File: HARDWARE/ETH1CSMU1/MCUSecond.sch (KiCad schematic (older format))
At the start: 23 parts

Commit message: Added ADC
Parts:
- removed C? (x2): 1u, symbol Device:C
- removed C? (x6): 100n, symbol Device:C
- removed FB? (x2): BEAD, symbol Device:Ferrite_Bead_Small
- removed U?: STM32F765VITx, Package_QFP:LQFP-100_14x14mm_P0.5mm, symbol MCU_ST_STM32F7:STM32F765VITx
- added C201, C203, C204, C205, C206, C207, C210, C211, C214, C215, C216, C217: 100n, symbol Device:C
- added C218: 1u, symbol Device:C
- added C219, C220: 2u2, symbol Device:C
- added FB201: Ferrite_Bead_Small, symbol Device:Ferrite_Bead_Small
- added R205: R, symbol Device:R
- added U202: STM32F746ZGTx, symbol stm32:STM32F746ZGTx
- gave numbers to parts that had none: 12
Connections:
- net labels added: MCU_3V3
- net labels removed: +3V3
- wire segments 146 -> 184
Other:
- moved on the sheet: C208, C209, C212, C213, J201, R202, R203, R204, U201, X201

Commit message: Commit
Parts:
- removed R204: R, symbol Device:R
- added FB202: MPZ2012S221A, SMD:R_0805_Symbol1, symbol Device:Ferrite_Bead_Small
- C201, C202, C203, C204, C205, C206, C207, C210, C211, C214, C215, C216, C217: footprint (none) -> SMD:C_0603_Symbol1
- C212: value 2u7 -> 100n; footprint (none) -> SMD:C_0603_Symbol1
- C213: value 2u7 -> 1u
- FB201: value Ferrite_Bead_Small -> MPZ2012S221A; footprint (none) -> SMD:R_0805_Symbol1
- R201: footprint (none) -> SMD:R_0603_Symbol1
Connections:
- net labels added: SECOND-I2C1_SCL, SECOND-I2C1_SDA, SECOND-NC-TDI, SECOND-NRST, SECOND-SWDCKL-TCK, SECOND-SWDIO-TMS, SECOND-SWO-TDO
- net labels removed: FGEN_FSELECT, FGEN_PSELECT, FGEN_SLEEP, I2C1_SCL, I2C1_SDA, NRST, POLARITY, QDAC_~CLR, QDAC_~LDAC, SIGN_SELECT, SPI2_MISO, SPI2_MOSI, SPI2_NSS, SPI2_SCK, SPI4_MOSI, SPI4_NSS1, SPI4_NSS2, SPI4_NSS3, SPI4_SCK, SPI6_MISO, SPI6_MOSI, SPI6_NSS1, SPI6_NSS2, SPI6_SCK, TCK, TDI, TDO, TMS, VDDA
- wire segments 184 -> 162
- no-connect marks 3 -> 2
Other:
- moved on the sheet: C201, C202, C203, C204, C205, C206, C207, C210, C211, C214, C215, C216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

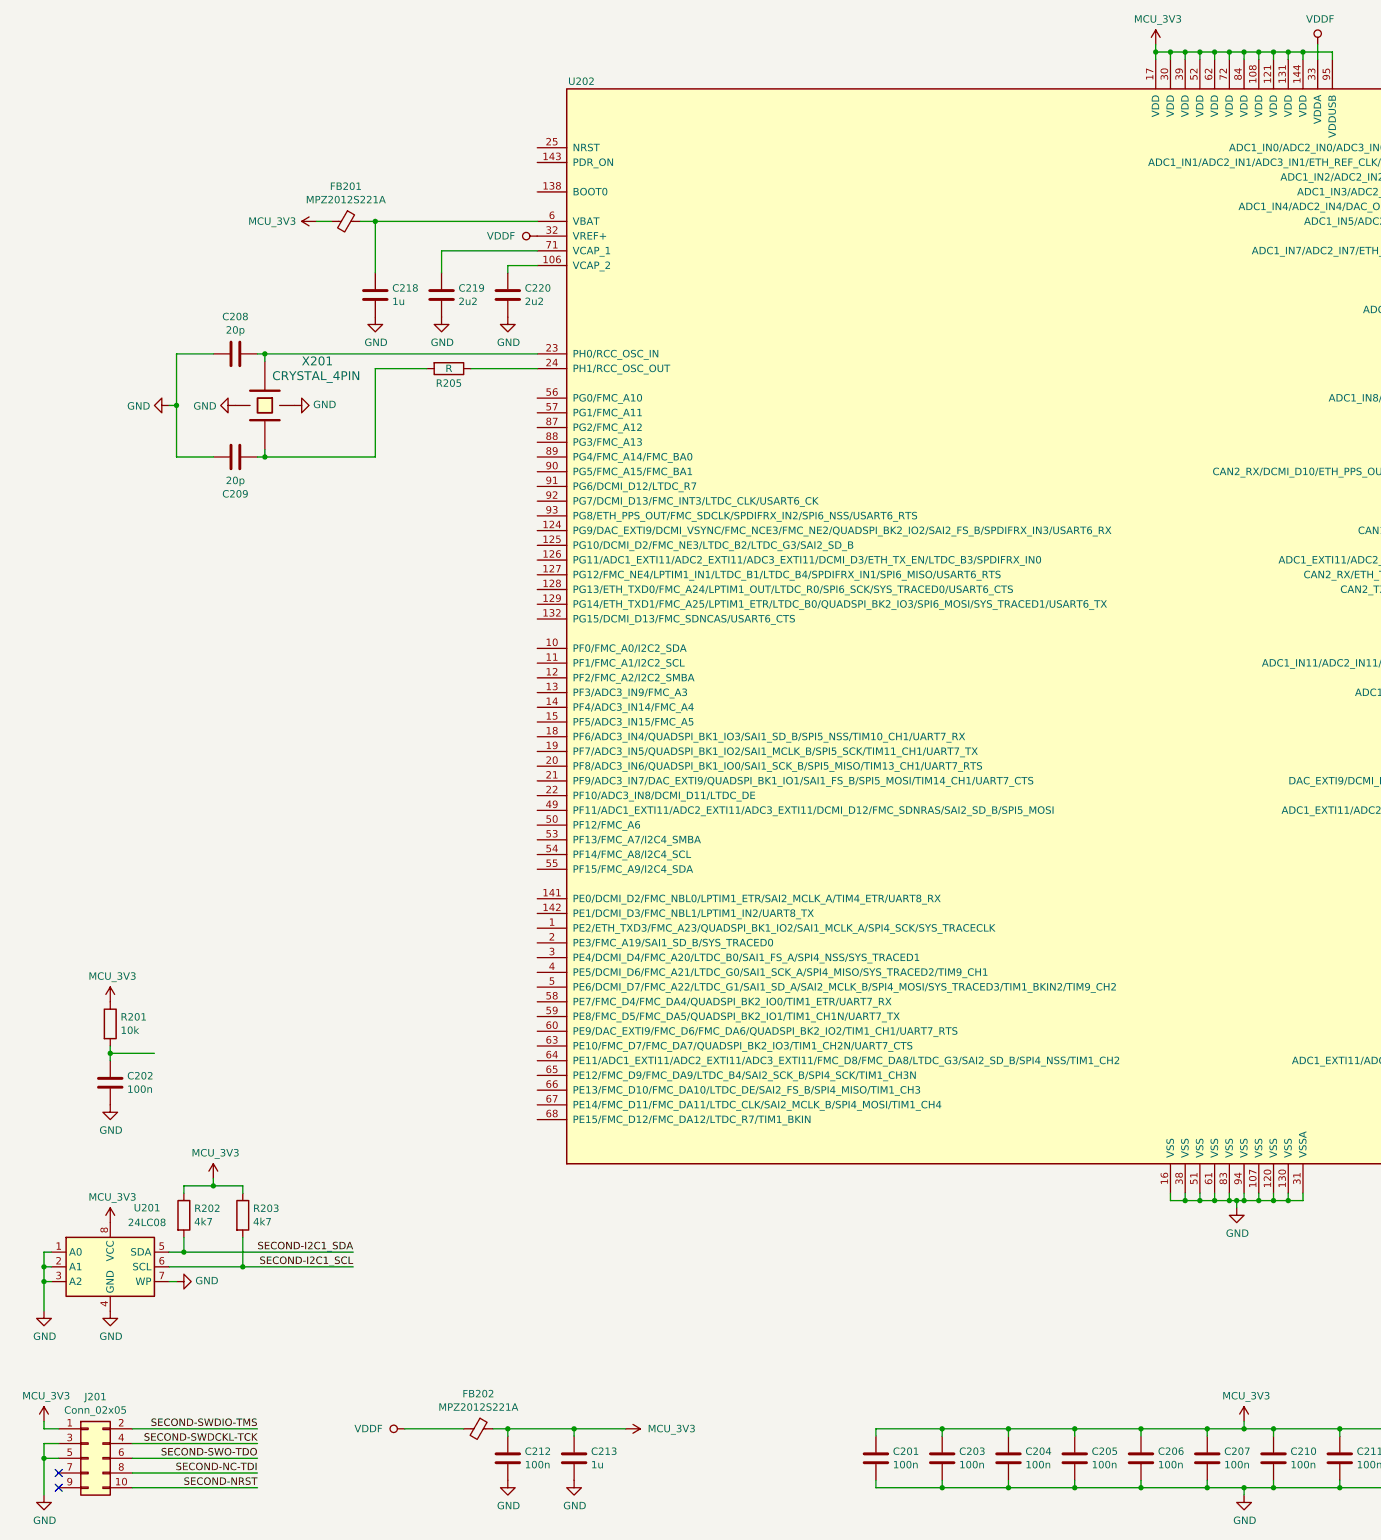
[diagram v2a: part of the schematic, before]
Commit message: Power schematic
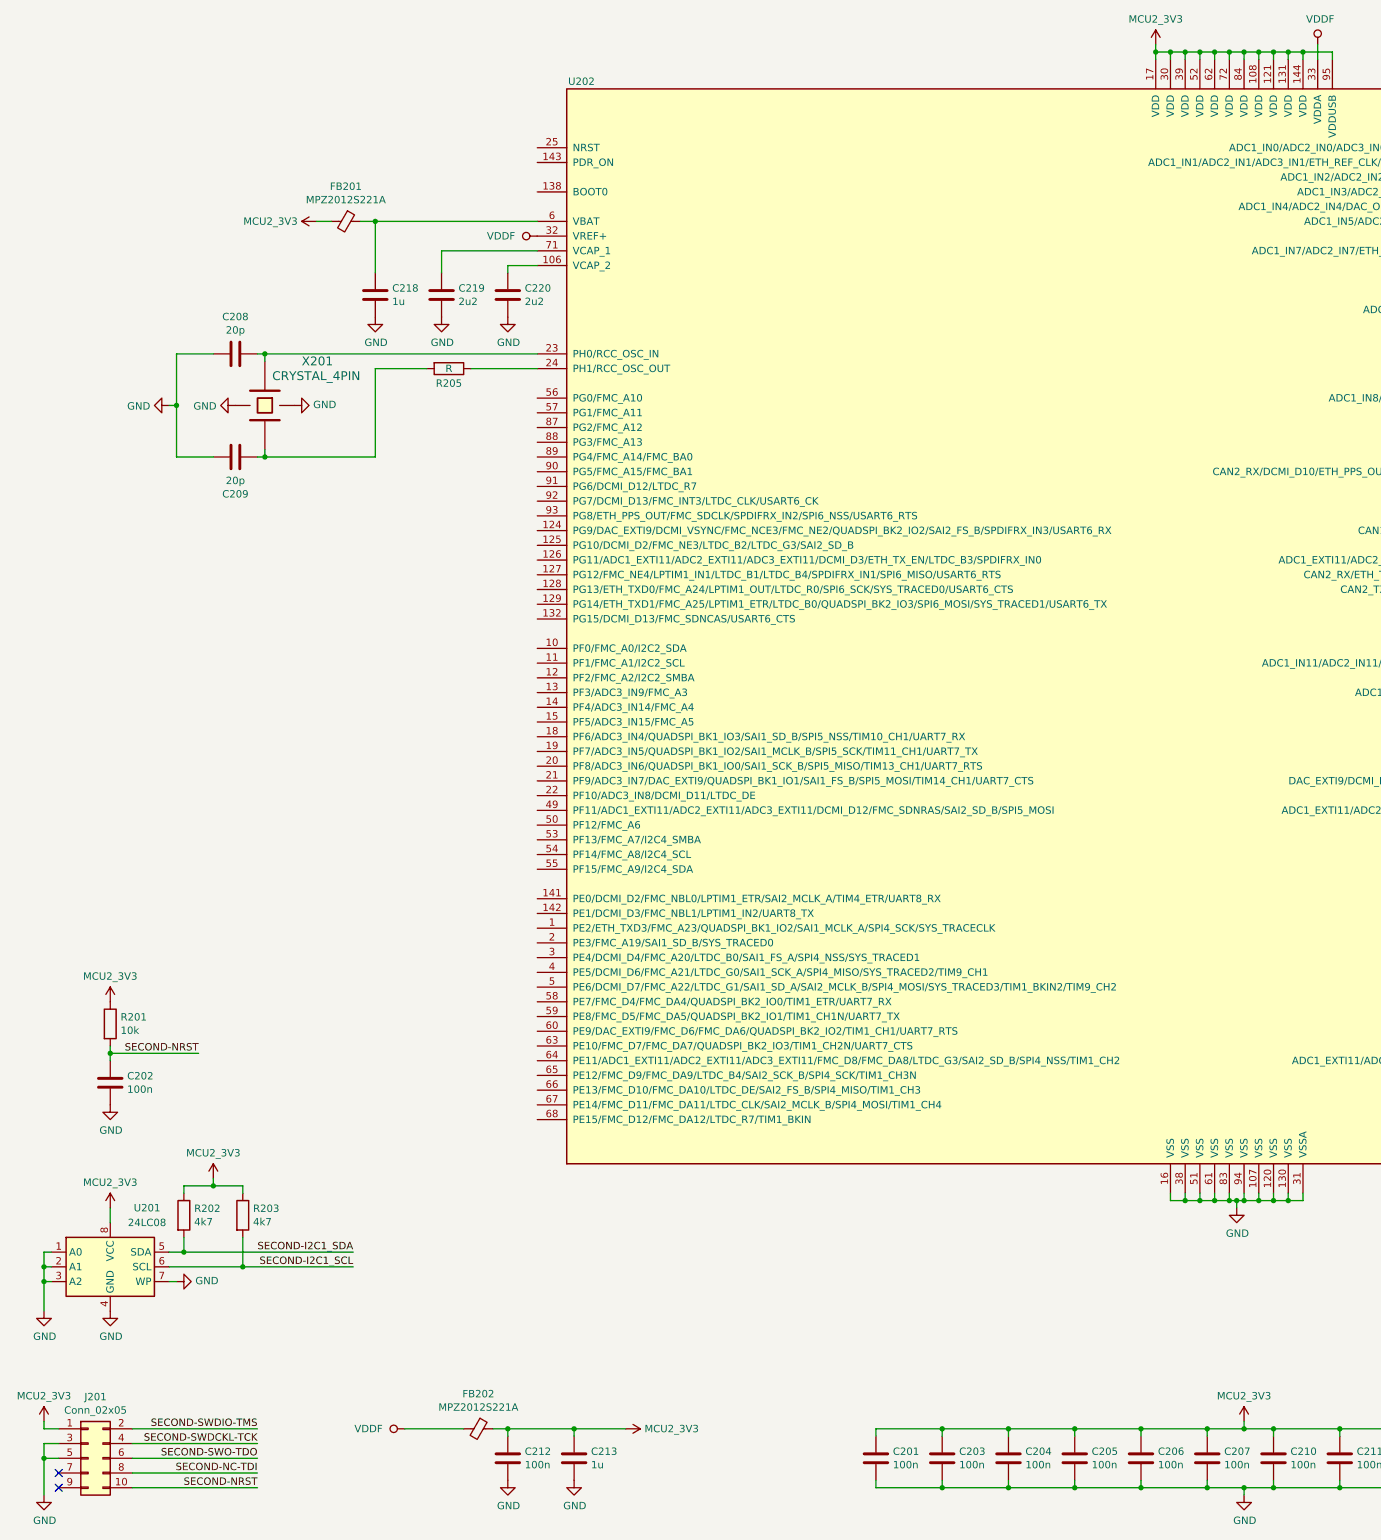
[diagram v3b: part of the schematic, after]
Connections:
- net SECOND-NRST: now also C202.1, R201.2
- net MCU_3V3 renamed MCU2_3V3
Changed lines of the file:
@@
 $Descr A3 16535 11693
 encoding utf-8
-Sheet 2 12
+Sheet 2 13
 Title ""
 Date ""
@@
 	2950 3250 2950 3850
 Wire Wire Line
-	1150 7900 1450 7900
-Wire Wire Line
 	8800 8950 8800 8900
 $Comp
@@
 	1    1600 9450
 	0    -1   -1   0
-$EndComp
-$Comp
-L power_local:MCU_3V3 #PWR0204
-U 1 1 5BE1AE38
-P 1150 7550
-F 0 "#PWR0204" H 1150 7400 50  0001 C CNN
-F 1 "MCU_3V3" H 1165 7723 50  0000 C CNN
-F 2 "" H 1150 7550 50  0000 C CNN
-F 3 "" H 1150 7550 50  0000 C CNN
-	1    1150 7550
-	1    0    0    -1
-$EndComp
-$Comp
-L power_local:MCU_3V3 #PWR0206
-U 1 1 5BE1AFD5
-P 1150 9050
-F 0 "#PWR0206" H 1150 8900 50  0001 C CNN
-F 1 "MCU_3V3" H 1165 9223 50  0000 C CNN
-F 2 "" H 1150 9050 50  0000 C CNN
-F 3 "" H 1150 9050 50  0000 C CNN
-	1    1150 9050
-	1    0    0    -1
-$EndComp
-$Comp
-L power_local:MCU_3V3 #PWR0211
-U 1 1 5BE1B10D
-P 1850 8750
-F 0 "#PWR0211" H 1850 8600 50  0001 C CNN
-F 1 "MCU_3V3" H 1865 8923 50  0000 C CNN
-F 2 "" H 1850 8750 50  0000 C CNN
-F 3 "" H 1850 8750 50  0000 C CNN
-	1    1850 8750
-	1    0    0    -1
-$EndComp
-$Comp
-L power_local:MCU_3V3 #PWR0202
-U 1 1 5BE1B195
-P 700 10400
-F 0 "#PWR0202" H 700 10250 50  0001 C CNN
-F 1 "MCU_3V3" H 715 10573 50  0000 C CNN
-F 2 "" H 700 10400 50  0000 C CNN
-F 3 "" H 700 10400 50  0000 C CNN
-	1    700  10400
-	1    0    0    -1
 $EndComp
 $Comp
@@
 Wire Wire Line
 	8850 10850 8600 10850
-$Comp
-L power_local:MCU_3V3 #PWR?
-U 1 1 5C00912F
-P 8850 10400
-AR Path="/5BE4235D/5C00912F" Ref="#PWR?"  Part="1"
-AR Path="/5BE0F4FE/5C00912F" Ref="#PWR0209"  Part="1"
-F 0 "#PWR0209" H 8850 10250 50  0001 C CNN
-F 1 "MCU_3V3" H 8865 10573 50  0000 C CNN
-F 2 "" H 8850 10400 50  0000 C CNN
-F 3 "" H 8850 10400 50  0000 C CNN
-	1    8850 10400
-	1    0    0    -1
-$EndComp
 Wire Wire Line
 	8850 10400 8850 10450
@@
 	9450 1100 9250 1100
 Connection ~ 9250 1100
-$Comp
-L power_local:MCU_3V3 #PWR0223
-U 1 1 5C05C691
-P 8250 1050
-F 0 "#PWR0223" H 8250 900 50  0001 C CNN
-F 1 "MCU_3V3" H 8265 1223 50  0000 C CNN
-F 2 "" H 8250 1050 50  0000 C CNN
-F 3 "" H 8250 1050 50  0000 C CNN
-	1    8250 1050
-	1    0    0    -1
-$EndComp
 Wire Wire Line
 	8250 1050 8250 1100
@@
 Wire Wire Line
 	9350 1050 9350 1150
-$Comp
-L power_local:MCU_3V3 #PWR?
-U 1 1 5C070F39
-P 2550 2250
-AR Path="/5BE4235D/5C070F39" Ref="#PWR?"  Part="1"
-AR Path="/5BE0F4FE/5C070F39" Ref="#PWR0214"  Part="1"
-F 0 "#PWR0214" H 2550 2100 50  0001 C CNN
-F 1 "MCU_3V3" V 2550 2550 50  0000 C CNN
-F 2 "" H 2550 2250 50  0000 C CNN
-F 3 "" H 2550 2250 50  0000 C CNN
-	1    2550 2250
-	0    -1   -1   0
-$EndComp
 $Comp
 L Device:C C?
@@
 Connection ~ 4300 10450
 $Comp
-L power_local:MCU_3V3 #PWR?
-U 1 1 5C0CDE62
-P 4650 10450
-AR Path="/5BE4235D/5C0CDE62" Ref="#PWR?"  Part="1"
-AR Path="/5BE0F4FE/5C0CDE62" Ref="#PWR0225"  Part="1"
-F 0 "#PWR0225" H 4650 10300 50  0001 C CNN
-F 1 "MCU_3V3" V 4650 10600 50  0000 L CNN
-F 2 "" H 4650 10450 50  0000 C CNN
-F 3 "" H 4650 10450 50  0000 C CNN
-	1    4650 10450
-	0    1    1    0
-$EndComp
-$Comp
 L power:VDDF #PWR0217
 U 1 1 5C0D7178
@@
 	0    -1   -1   0
 $EndComp
+Text Label 1750 7900 2    50   ~ 0
+SECOND-NRST
+Wire Wire Line
+	1150 7900 1750 7900
+$Comp
+L power_local:MCU2_3V3 #PWR?
+U 1 1 5C42AB18
+P 1850 8750
+F 0 "#PWR?" H 1850 8650 50  0001 C CNN
+F 1 "MCU2_3V3" H 1850 8923 50  0000 C CNN
+F 2 "" H 1850 8750 50  0000 C CNN
+F 3 "" H 1850 8750 50  0000 C CNN
+	1    1850 8750
+	1    0    0    -1
+$EndComp
+$Comp
+L power_local:MCU2_3V3 #PWR?
+U 1 1 5C42ACBA
+P 1150 8950
+F 0 "#PWR?" H 1150 8850 50  0001 C CNN
+F 1 "MCU2_3V3" H 1150 9123 50  0000 C CNN
+F 2 "" H 1150 8950 50  0000 C CNN
+F 3 "" H 1150 8950 50  0000 C CNN
+	1    1150 8950
+	1    0    0    -1
+$EndComp
+Wire Wire Line
+	1150 8950 1150 9050
+$Comp
+L power_local:MCU2_3V3 #PWR?
+U 1 1 5C4315B4
+P 1150 7550
+F 0 "#PWR?" H 1150 7450 50  0001 C CNN
+F 1 "MCU2_3V3" H 1150 7723 50  0000 C CNN
+F 2 "" H 1150 7550 50  0000 C CNN
+F 3 "" H 1150 7550 50  0000 C CNN
+	1    1150 7550
+	1    0    0    -1
+$EndComp
+$Comp
+L power_local:MCU2_3V3 #PWR?
+U 1 1 5C431709
+P 700 10400
+F 0 "#PWR?" H 700 10300 50  0001 C CNN
+F 1 "MCU2_3V3" H 700 10573 50  0000 C CNN
+F 2 "" H 700 10400 50  0000 C CNN
+F 3 "" H 700 10400 50  0000 C CNN
+	1    700  10400
+	1    0    0    -1
+$EndComp
+$Comp
+L power_local:MCU2_3V3 #PWR?
+U 1 1 5C43189A
+P 8850 10400
+F 0 "#PWR?" H 8850 10300 50  0001 C CNN
+F 1 "MCU2_3V3" H 8850 10573 50  0000 C CNN
+F 2 "" H 8850 10400 50  0000 C CNN
+F 3 "" H 8850 10400 50  0000 C CNN
+	1    8850 10400
+	1    0    0    -1
+$EndComp
+$Comp
+L power_local:MCU2_3V3 #PWR?
+U 1 1 5C431A2B
+P 4650 10450
+F 0 "#PWR?" H 4650 10350 50  0001 C CNN
+F 1 "MCU2_3V3" V 4650 10578 50  0000 L CNN
+F 2 "" H 4650 10450 50  0000 C CNN
+F 3 "" H 4650 10450 50  0000 C CNN
+	1    4650 10450
+	0    1    1    0
+$EndComp
+$Comp
+L power_local:MCU2_3V3 #PWR?
+U 1 1 5C431CF3
+P 2550 2250
+F 0 "#PWR?" H 2550 2150 50  0001 C CNN
+F 1 "MCU2_3V3" V 2550 2377 50  0000 L CNN
+F 2 "" H 2550 2250 50  0000 C CNN
+F 3 "" H 2550 2250 50  0000 C CNN
+	1    2550 2250
+	0    -1   -1   0
+$EndComp
+$Comp
+L power_local:MCU2_3V3 #PWR?
+U 1 1 5C43210A
+P 8250 1050
+F 0 "#PWR?" H 8250 950 50  0001 C CNN
+F 1 "MCU2_3V3" H 8250 1223 50  0000 C CNN
+F 2 "" H 8250 1050 50  0000 C CNN
+F 3 "" H 8250 1050 50  0000 C CNN
+	1    8250 1050
+	1    0    0    -1
+$EndComp
 $EndSCHEMATC

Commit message: Footprints
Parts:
- C208, C209: footprint (none) -> Capacitors_SMD:C_0603
- J201: footprint (none) -> Pin_Headers:Pin_Header_Straight_2x05_Pitch1.27mm
- U201: footprint (none) -> Housings_SSOP:MSOP-8_3x3mm_Pitch0.65mm
- U202: footprint (none) -> SMD:TQFP-144
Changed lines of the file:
@@
 F 0 "U201" H 1400 9750 50  0000 C CNN
 F 1 "24LC08" H 1400 9650 50  0000 C CNN
-F 2 "" H 1150 9350 50  0001 C CNN
+F 2 "Housings_SSOP:MSOP-8_3x3mm_Pitch0.65mm" H 1150 9350 50  0001 C CNN
 F 3 "http://ww1.microchip.com/downloads/en/DeviceDoc/21710J.pdf" H 1150 9350 50  0001 C CNN
 	1    1150 9350
@@
 F 0 "C208" V 1748 3150 50  0000 C CNN
 F 1 "20p" V 1839 3150 50  0000 C CNN
-F 2 "" H 2038 3000 50  0001 C CNN
+F 2 "Capacitors_SMD:C_0603" H 2038 3000 50  0001 C CNN
 F 3 "~" H 2000 3150 50  0001 C CNN
 	1    2000 3150
@@
 F 0 "C209" V 2252 3850 50  0000 C CNN
 F 1 "20p" V 2161 3850 50  0000 C CNN
-F 2 "" H 2038 3700 50  0001 C CNN
+F 2 "Capacitors_SMD:C_0603" H 2038 3700 50  0001 C CNN
 F 3 "~" H 2000 3850 50  0001 C CNN
 	1    2000 3850
@@
 F 0 "J201" H 1050 11067 50  0000 C CNN
 F 1 "Conn_02x05" H 1050 10976 50  0000 C CNN
-F 2 "" H 1000 10650 50  0001 C CNN
+F 2 "Pin_Headers:Pin_Header_Straight_2x05_Pitch1.27mm" H 1000 10650 50  0001 C CNN
 F 3 "~" H 1000 10650 50  0001 C CNN
 	1    1000 10650
@@
 F 0 "U202" H 4350 8800 50  0000 C CNN
 F 1 "STM32F746ZGTx" H 13150 8800 50  0000 C CNN
-F 2 "" H 13450 8725 50  0001 R TNN
+F 2 "SMD:TQFP-144" H 13450 8725 50  0001 R TNN
 F 3 "http://www.st.com/st-web-ui/static/active/en/resource/technical/document/datasheet/DM00166116.pdf" H 8850 5050 50  0001 C CNN
 	1    8850 5050
@@
 	1150 7900 1750 7900
 $Comp
-L power_local:MCU2_3V3 #PWR?
+L power_local:MCU2_3V3 #PWR0115
 U 1 1 5C42AB18
 P 1850 8750
-F 0 "#PWR?" H 1850 8650 50  0001 C CNN
+F 0 "#PWR0115" H 1850 8650 50  0001 C CNN
 F 1 "MCU2_3V3" H 1850 8923 50  0000 C CNN
 F 2 "" H 1850 8750 50  0000 C CNN
@@
 $EndComp
 $Comp
-L power_local:MCU2_3V3 #PWR?
+L power_local:MCU2_3V3 #PWR0116
 U 1 1 5C42ACBA
 P 1150 8950
-F 0 "#PWR?" H 1150 8850 50  0001 C CNN
+F 0 "#PWR0116" H 1150 8850 50  0001 C CNN
 F 1 "MCU2_3V3" H 1150 9123 50  0000 C CNN
 F 2 "" H 1150 8950 50  0000 C CNN
@@
 	1150 8950 1150 9050
 $Comp
-L power_local:MCU2_3V3 #PWR?
+L power_local:MCU2_3V3 #PWR0117
 U 1 1 5C4315B4
 P 1150 7550
-F 0 "#PWR?" H 1150 7450 50  0001 C CNN
+F 0 "#PWR0117" H 1150 7450 50  0001 C CNN
 F 1 "MCU2_3V3" H 1150 7723 50  0000 C CNN
 F 2 "" H 1150 7550 50  0000 C CNN
@@
 $EndComp
 $Comp
-L power_local:MCU2_3V3 #PWR?
+L power_local:MCU2_3V3 #PWR0118
 U 1 1 5C431709
 P 700 10400
-F 0 "#PWR?" H 700 10300 50  0001 C CNN
+F 0 "#PWR0118" H 700 10300 50  0001 C CNN
 F 1 "MCU2_3V3" H 700 10573 50  0000 C CNN
 F 2 "" H 700 10400 50  0000 C CNN
@@
 $EndComp
 $Comp
-L power_local:MCU2_3V3 #PWR?
+L power_local:MCU2_3V3 #PWR0119
 U 1 1 5C43189A
 P 8850 10400
-F 0 "#PWR?" H 8850 10300 50  0001 C CNN
+F 0 "#PWR0119" H 8850 10300 50  0001 C CNN
 F 1 "MCU2_3V3" H 8850 10573 50  0000 C CNN
 F 2 "" H 8850 10400 50  0000 C CNN
@@
 $EndComp
 $Comp
-L power_local:MCU2_3V3 #PWR?
+L power_local:MCU2_3V3 #PWR0120
 U 1 1 5C431A2B
 P 4650 10450
-F 0 "#PWR?" H 4650 10350 50  0001 C CNN
+F 0 "#PWR0120" H 4650 10350 50  0001 C CNN
 F 1 "MCU2_3V3" V 4650 10578 50  0000 L CNN
 F 2 "" H 4650 10450 50  0000 C CNN
@@
 $EndComp
 $Comp
-L power_local:MCU2_3V3 #PWR?
+L power_local:MCU2_3V3 #PWR0121
 U 1 1 5C431CF3
 P 2550 2250
-F 0 "#PWR?" H 2550 2150 50  0001 C CNN
+F 0 "#PWR0121" H 2550 2150 50  0001 C CNN
 F 1 "MCU2_3V3" V 2550 2377 50  0000 L CNN
 F 2 "" H 2550 2250 50  0000 C CNN
@@
 $EndComp
 $Comp
-L power_local:MCU2_3V3 #PWR?
+L power_local:MCU2_3V3 #PWR0122
 U 1 1 5C43210A
 P 8250 1050
-F 0 "#PWR?" H 8250 950 50  0001 C CNN
+F 0 "#PWR0122" H 8250 950 50  0001 C CNN
 F 1 "MCU2_3V3" H 8250 1223 50  0000 C CNN
 F 2 "" H 8250 1050 50  0000 C CNN

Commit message: Footprint selection
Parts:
- R202, R203: footprint (none) -> SMD:R_0603_Symbol6
- R205: value R -> 200; footprint (none) -> Resistors_SMD:R_0603
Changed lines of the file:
@@
 F 0 "R202" H 1720 9046 50  0000 L CNN
 F 1 "4k7" H 1720 8955 50  0000 L CNN
-F 2 "" V 1580 9000 50  0001 C CNN
+F 2 "SMD:R_0603_Symbol6" V 1580 9000 50  0001 C CNN
 F 3 "~" H 1650 9000 50  0001 C CNN
 	1    1650 9000
@@
 F 0 "R203" H 2120 9046 50  0000 L CNN
 F 1 "4k7" H 2120 8955 50  0000 L CNN
-F 2 "" V 1980 9000 50  0001 C CNN
+F 2 "SMD:R_0603_Symbol6" V 1980 9000 50  0001 C CNN
 F 3 "~" H 2050 9000 50  0001 C CNN
 	1    2050 9000
@@
 P 3450 3250
 F 0 "R205" V 3550 3250 50  0000 C CNN
-F 1 "R" V 3450 3250 50  0000 C CNN
-F 2 "" V 3380 3250 50  0001 C CNN
+F 1 "200" V 3650 3250 50  0000 C CNN
+F 2 "Resistors_SMD:R_0603" V 3380 3250 50  0001 C CNN
 F 3 "~" H 3450 3250 50  0001 C CNN
 	1    3450 3250
